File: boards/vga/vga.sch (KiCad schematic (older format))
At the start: 80 parts, among them J1 Conn_02x20_Odd_Even, J2 L77HDE15SD1CH4RHNVGA, Q1 BSS84AK, U1 SN74LV161APW, U10 62256-TSOP, U11 SN74LV161APW, U12 SN74LV161APW, U13 SN74LV244APW, U14 SN74LV20APW, U15 74LV32APWJ, U16 74LV08APWJ, U17 AT28C256-PLCC32, U18 SN74LV273APW, U19 SN74LV273APW, U2 SN74LV161APW, U20 CD74AC151M96, U21 SN74LV157APW, U22 SN74LV10APW, U23 SN74LV74APW, U24 SN74LV00APW, U25 74LV32APWJ, U26 SN74LV21APW, U27 SN74AHC1G86DBVR, U28 74LV32APWJ, U29 74LV08APWJ, U3 SN74LV157APW, U30 SN74LV74APW, U4 SN74LV157APW, U5 SN74LV157APW, U6 SN74LV161APW, U7 SN74LV161APW, U8 SN74LV244APW, U9 62256-TSOP, X1 MXO45HS-3C-25M1750

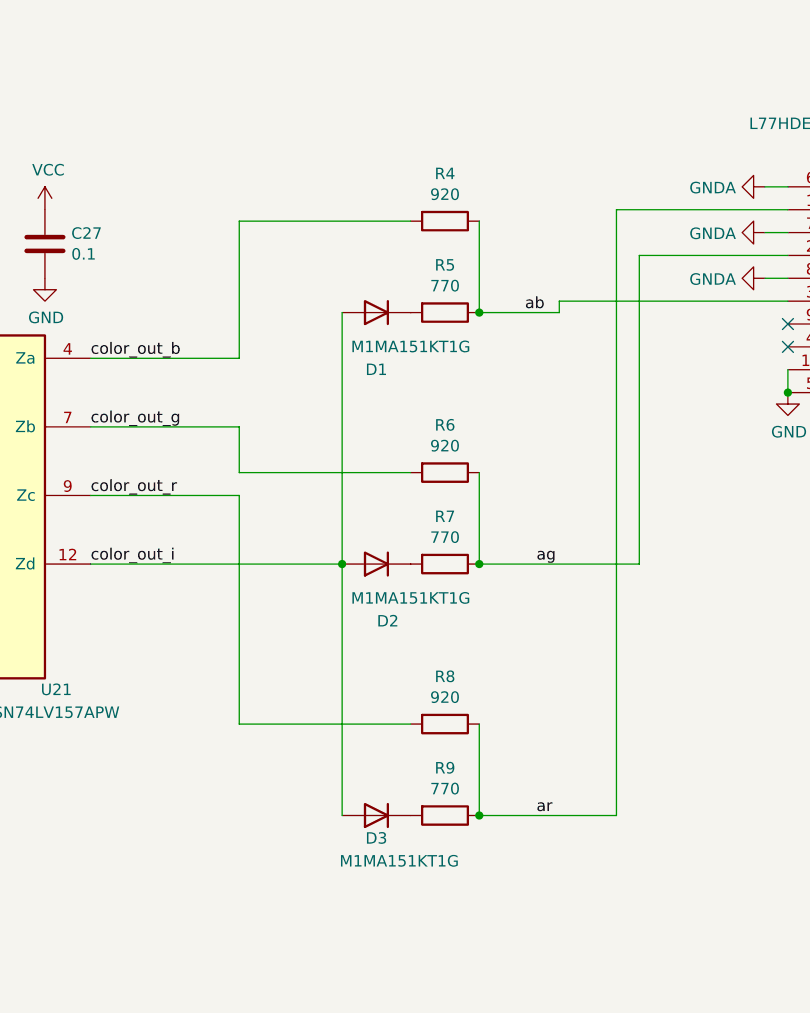
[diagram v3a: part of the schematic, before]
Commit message: VGA: DAC diode array and trim potentiometers
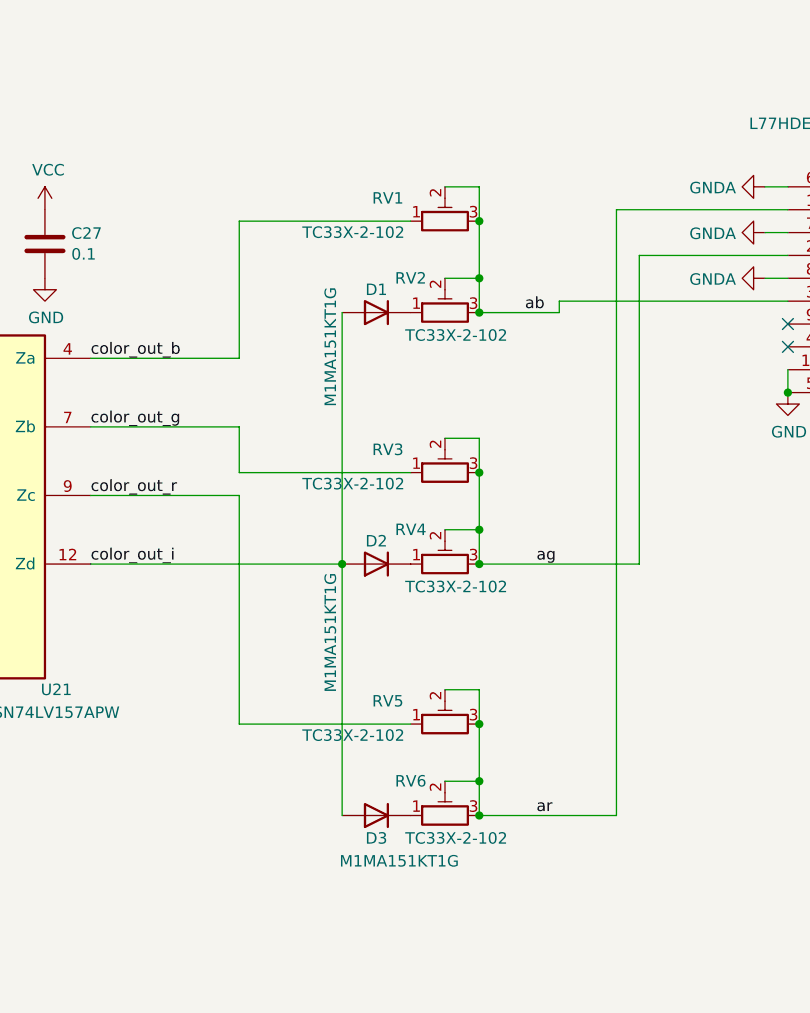
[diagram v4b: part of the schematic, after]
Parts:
- removed R4, R6, R8: 920, symbol Device:R
- removed R5, R7, R9: 770, symbol Device:R
- added RV1, RV2, RV3, RV4, RV5, RV6: TC33X-2-102, Potentiometer_SMD:Potentiometer_Bourns_TC33X_Vertical, symbol Device:R_POT_TRIM
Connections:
- net ab: now also RV1.2, RV1.3, RV2.2, RV2.3
- net ag: now also RV3.2, RV3.3, RV4.2, RV4.3
- net ar: now also RV5.2, RV5.3, RV6.2, RV6.3
- net color_out_b: now also RV1.1
- net color_out_g: now also RV3.1
- net color_out_r: now also RV5.1
- net at D1.1 (K): now also RV2.1
- net at D2.1 (K): now also RV4.1
- net at D3.1 (K): now also RV6.1
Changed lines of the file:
@@
 U 1 1 5FEACDCC
 P 19700 4450
-F 0 "D1" H 19700 4700 50  0000 C CNN
-F 1 "M1MA151KT1G" H 19550 4600 50  0000 C CNN
+F 0 "D1" H 19700 4350 50  0000 C CNN
+F 1 "M1MA151KT1G" V 19900 4600 50  0000 C CNN
 F 2 "Diode_SMD:D_SOT-23_ANK" H 19700 4450 50  0001 C CNN
 F 3 "https://www.mouser.de/datasheet/2/308/M1MA151KT1_D-1810723.pdf" H 19700 4450 50  0001 C CNN
@@
 	-1   0    0    1
 $EndComp
-$Comp
-L Device:R R5
-U 1 1 5FEB1B5A
-P 20000 4450
-F 0 "R5" V 19793 4450 50  0000 C CNN
-F 1 "770" V 19884 4450 50  0000 C CNN
-F 2 "" V 19930 4450 50  0001 C CNN
-F 3 "~" H 20000 4450 50  0001 C CNN
-	1    20000 4450
-	0    1    1    0
-$EndComp
-$Comp
-L Device:R R4
-U 1 1 5FEB20CB
-P 20000 4050
-F 0 "R4" V 19793 4050 50  0000 C CNN
-F 1 "920" V 19884 4050 50  0000 C CNN
-F 2 "" V 19930 4050 50  0001 C CNN
-F 3 "~" H 20000 4050 50  0001 C CNN
-	1    20000 4050
-	0    1    1    0
-$EndComp
-Wire Wire Line
-	20150 4450 20150 4050
-Connection ~ 20150 4450
+Wire Wire Line
+	20150 4450 20150 4300
 $Comp
 L power:GNDA #PWR0166
@@
 U 1 1 5FF3DA39
 P 19700 5550
-F 0 "D2" H 19650 5800 50  0000 C CNN
-F 1 "M1MA151KT1G" H 19550 5700 50  0000 C CNN
+F 0 "D2" H 19700 5450 50  0000 C CNN
+F 1 "M1MA151KT1G" V 19900 5850 50  0000 C CNN
 F 2 "Diode_SMD:D_SOT-23_ANK" H 19700 5550 50  0001 C CNN
 F 3 "https://www.mouser.de/datasheet/2/308/M1MA151KT1_D-1810723.pdf" H 19700 5550 50  0001 C CNN
@@
 	-1   0    0    1
 $EndComp
-$Comp
-L Device:R R7
-U 1 1 5FF3DA3F
-P 20000 5550
-F 0 "R7" V 19793 5550 50  0000 C CNN
-F 1 "770" V 19884 5550 50  0000 C CNN
-F 2 "" V 19930 5550 50  0001 C CNN
-F 3 "~" H 20000 5550 50  0001 C CNN
-	1    20000 5550
-	0    1    1    0
-$EndComp
-$Comp
-L Device:R R6
-U 1 1 5FF3DA45
-P 20000 5150
-F 0 "R6" V 19793 5150 50  0000 C CNN
-F 1 "920" V 19884 5150 50  0000 C CNN
-F 2 "" V 19930 5150 50  0001 C CNN
-F 3 "~" H 20000 5150 50  0001 C CNN
-	1    20000 5150
-	0    1    1    0
-$EndComp
-Wire Wire Line
-	20150 5550 20150 5150
-Connection ~ 20150 5550
+Wire Wire Line
+	20150 5550 20150 5400
 $Comp
 L Device:D D3
@@
 	-1   0    0    1
 $EndComp
-$Comp
-L Device:R R9
-U 1 1 5FF5B8A6
-P 20000 6650
-F 0 "R9" V 19793 6650 50  0000 C CNN
-F 1 "770" V 19884 6650 50  0000 C CNN
-F 2 "" V 19930 6650 50  0001 C CNN
-F 3 "~" H 20000 6650 50  0001 C CNN
-	1    20000 6650
-	0    1    1    0
-$EndComp
-$Comp
-L Device:R R8
-U 1 1 5FF5B8AC
-P 20000 6250
-F 0 "R8" V 19793 6250 50  0000 C CNN
-F 1 "920" V 19884 6250 50  0000 C CNN
-F 2 "" V 19930 6250 50  0001 C CNN
-F 3 "~" H 20000 6250 50  0001 C CNN
-	1    20000 6250
-	0    1    1    0
-$EndComp
-Wire Wire Line
-	20150 6650 20150 6250
-Connection ~ 20150 6650
+Wire Wire Line
+	20150 6650 20150 6500
 Wire Wire Line
 	19550 6650 19550 5550
@@
 ar
 NoConn ~ 21500 4500
+$Comp
+L Device:R_POT_TRIM RV1
+U 1 1 5FD795FD
+P 20000 4050
+F 0 "RV1" V 20100 4300 50  0000 C CNN
+F 1 "TC33X-2-102" V 19950 4450 50  0000 C CNN
+F 2 "Potentiometer_SMD:Potentiometer_Bourns_TC33X_Vertical" H 20000 4050 50  0001 C CNN
+F 3 "https://www.mouser.de/datasheet/2/54/tc33-778219.pdf" H 20000 4050 50  0001 C CNN
+	1    20000 4050
+	0    -1   -1   0
+$EndComp
+$Comp
+L Device:R_POT_TRIM RV2
+U 1 1 5FD7B4C1
+P 20000 4450
+F 0 "RV2" V 20150 4600 50  0000 C CNN
+F 1 "TC33X-2-102" V 19900 4400 50  0000 C CNN
+F 2 "Potentiometer_SMD:Potentiometer_Bourns_TC33X_Vertical" H 20000 4450 50  0001 C CNN
+F 3 "https://www.mouser.de/datasheet/2/54/tc33-778219.pdf" H 20000 4450 50  0001 C CNN
+	1    20000 4450
+	0    -1   -1   0
+$EndComp
+Connection ~ 20150 4450
+$Comp
+L Device:R_POT_TRIM RV3
+U 1 1 5FD7D4C9
+P 20000 5150
+F 0 "RV3" V 20100 5400 50  0000 C CNN
+F 1 "TC33X-2-102" V 19950 5550 50  0000 C CNN
+F 2 "Potentiometer_SMD:Potentiometer_Bourns_TC33X_Vertical" H 20000 5150 50  0001 C CNN
+F 3 "https://www.mouser.de/datasheet/2/54/tc33-778219.pdf" H 20000 5150 50  0001 C CNN
+	1    20000 5150
+	0    -1   -1   0
+$EndComp
+$Comp
+L Device:R_POT_TRIM RV4
+U 1 1 5FD7DC16
+P 20000 5550
+F 0 "RV4" V 20150 5700 50  0000 C CNN
+F 1 "TC33X-2-102" V 19900 5500 50  0000 C CNN
+F 2 "Potentiometer_SMD:Potentiometer_Bourns_TC33X_Vertical" H 20000 5550 50  0001 C CNN
+F 3 "https://www.mouser.de/datasheet/2/54/tc33-778219.pdf" H 20000 5550 50  0001 C CNN
+	1    20000 5550
+	0    -1   -1   0
+$EndComp
+Connection ~ 20150 5550
+$Comp
+L Device:R_POT_TRIM RV6
+U 1 1 5FD7E9C9
+P 20000 6650
+F 0 "RV6" V 20150 6800 50  0000 C CNN
+F 1 "TC33X-2-102" V 19900 6600 50  0000 C CNN
+F 2 "Potentiometer_SMD:Potentiometer_Bourns_TC33X_Vertical" H 20000 6650 50  0001 C CNN
+F 3 "https://www.mouser.de/datasheet/2/54/tc33-778219.pdf" H 20000 6650 50  0001 C CNN
+	1    20000 6650
+	0    -1   -1   0
+$EndComp
+Connection ~ 20150 6650
+$Comp
+L Device:R_POT_TRIM RV5
+U 1 1 5FD7F2A0
+P 20000 6250
+F 0 "RV5" V 20100 6500 50  0000 C CNN
+F 1 "TC33X-2-102" V 19950 6650 50  0000 C CNN
+F 2 "Potentiometer_SMD:Potentiometer_Bourns_TC33X_Vertical" H 20000 6250 50  0001 C CNN
+F 3 "https://www.mouser.de/datasheet/2/54/tc33-778219.pdf" H 20000 6250 50  0001 C CNN
+	1    20000 6250
+	0    -1   -1   0
+$EndComp
+Wire Wire Line
+	20000 6100 20150 6100
+Wire Wire Line
+	20150 6100 20150 6250
+Connection ~ 20150 6250
+Wire Wire Line
+	20000 6500 20150 6500
+Connection ~ 20150 6500
+Wire Wire Line
+	20150 6500 20150 6250
+Wire Wire Line
+	20000 5400 20150 5400
+Connection ~ 20150 5400
+Wire Wire Line
+	20150 5400 20150 5150
+Wire Wire Line
+	20000 5000 20150 5000
+Wire Wire Line
+	20150 5000 20150 5150
+Connection ~ 20150 5150
+Wire Wire Line
+	20000 4300 20150 4300
+Connection ~ 20150 4300
+Wire Wire Line
+	20150 4300 20150 4050
+Wire Wire Line
+	20000 3900 20150 3900
+Wire Wire Line
+	20150 3900 20150 4050
 Wire Bus Line
 	11050 5150 11050 5850
@@
 Wire Bus Line
 	6050 4500 6050 10250
+Connection ~ 20150 4050
 $EndSCHEMATC

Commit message: VGA: big capacitor
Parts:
- removed D1, D2, D3: M1MA151KT1G, Diode_SMD:D_SOT-23_ANK, symbol Device:D
- added C31: TAJD476M016UNJV, Capacitor_Tantalum_SMD:CP_EIA-7343-40_Kemet-Y, symbol Device:CP
- added D1: BAS16TW, Package_TO_SOT_SMD:SOT-363_SC-70-6, symbol Diode:BAS16TW
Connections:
- net GND: now also C31.2
- net VCC: now also C31.1
- net color_out_i: now also D1.1 (A), D1.2 (A), D1.3 (A)
- net at RV2.1: now also D1.6 (K)
- net at RV4.1: now also D1.5 (K)
- net at RV6.1: now also D1.4 (K)
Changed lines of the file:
@@
 Text Label 22100 4600 0    50   ~ 0
 vsync_out
-$Comp
-L Device:D D1
-U 1 1 5FEACDCC
-P 19700 4450
-F 0 "D1" H 19700 4350 50  0000 C CNN
-F 1 "M1MA151KT1G" V 19900 4600 50  0000 C CNN
-F 2 "Diode_SMD:D_SOT-23_ANK" H 19700 4450 50  0001 C CNN
-F 3 "https://www.mouser.de/datasheet/2/308/M1MA151KT1_D-1810723.pdf" H 19700 4450 50  0001 C CNN
-	1    19700 4450
-	-1   0    0    1
-$EndComp
 Wire Wire Line
 	20150 4450 20150 4300
@@
 Wire Wire Line
 	21400 4100 21500 4100
-$Comp
-L Device:D D2
-U 1 1 5FF3DA39
-P 19700 5550
-F 0 "D2" H 19700 5450 50  0000 C CNN
-F 1 "M1MA151KT1G" V 19900 5850 50  0000 C CNN
-F 2 "Diode_SMD:D_SOT-23_ANK" H 19700 5550 50  0001 C CNN
-F 3 "https://www.mouser.de/datasheet/2/308/M1MA151KT1_D-1810723.pdf" H 19700 5550 50  0001 C CNN
-	1    19700 5550
-	-1   0    0    1
-$EndComp
 Wire Wire Line
 	20150 5550 20150 5400
-$Comp
-L Device:D D3
-U 1 1 5FF5B8A0
-P 19700 6650
-F 0 "D3" H 19700 6750 50  0000 C CNN
-F 1 "M1MA151KT1G" H 19600 6850 50  0000 C CNN
-F 2 "Diode_SMD:D_SOT-23_ANK" H 19700 6650 50  0001 C CNN
-F 3 "https://www.mouser.de/datasheet/2/308/M1MA151KT1_D-1810723.pdf" H 19700 6650 50  0001 C CNN
-	1    19700 6650
-	-1   0    0    1
-$EndComp
 Wire Wire Line
 	20150 6650 20150 6500
@@
 	6050 4500 6050 10250
 Connection ~ 20150 4050
+$Comp
+L Diode:BAS16TW D1
+U 1 1 5FE760D6
+P 19700 4450
+F 0 "D1" H 19850 4350 50  0000 C CNN
+F 1 "BAS16TW" V 19900 4600 50  0000 C CNN
+F 2 "Package_TO_SOT_SMD:SOT-363_SC-70-6" H 19700 4275 50  0001 C CNN
+F 3 "http://www.diodes.com/datasheets/ds30154.pdf" H 19700 4550 50  0001 C CNN
+	1    19700 4450
+	-1   0    0    1
+$EndComp
+$Comp
+L Diode:BAS16TW D1
+U 2 1 5FE78E2D
+P 19700 5550
+F 0 "D1" H 19950 5450 50  0000 C CNN
+F 1 "BAS16TW" V 19900 5750 50  0000 C CNN
+F 2 "Package_TO_SOT_SMD:SOT-363_SC-70-6" H 19700 5375 50  0001 C CNN
+F 3 "http://www.diodes.com/datasheets/ds30154.pdf" H 19700 5650 50  0001 C CNN
+	2    19700 5550
+	-1   0    0    1
+$EndComp
+$Comp
+L Diode:BAS16TW D1
+U 3 1 5FE7C453
+P 19700 6650
+F 0 "D1" H 19950 6650 50  0000 C CNN
+F 1 "BAS16TW" H 19850 6750 50  0000 C CNN
+F 2 "Package_TO_SOT_SMD:SOT-363_SC-70-6" H 19700 6475 50  0001 C CNN
+F 3 "http://www.diodes.com/datasheets/ds30154.pdf" H 19700 6750 50  0001 C CNN
+	3    19700 6650
+	-1   0    0    1
+$EndComp
+$Comp
+L Device:CP C31
+U 1 1 5FE890D9
+P 1800 4200
+F 0 "C31" H 1918 4246 50  0000 L CNN
+F 1 "TAJD476M016UNJV" H 1918 4155 50  0000 L CNN
+F 2 "Capacitor_Tantalum_SMD:CP_EIA-7343-40_Kemet-Y" H 1838 4050 50  0001 C CNN
+F 3 "~" H 1800 4200 50  0001 C CNN
+	1    1800 4200
+	1    0    0    -1
+$EndComp
+$Comp
+L power:VCC #PWR0171
+U 1 1 5FE8AE40
+P 1800 4050
+F 0 "#PWR0171" H 1800 3900 50  0001 C CNN
+F 1 "VCC" V 1815 4177 50  0000 L CNN
+F 2 "" H 1800 4050 50  0001 C CNN
+F 3 "" H 1800 4050 50  0001 C CNN
+	1    1800 4050
+	1    0    0    -1
+$EndComp
+$Comp
+L power:GND #PWR0172
+U 1 1 5FE8B51C
+P 1800 4350
+F 0 "#PWR0172" H 1800 4100 50  0001 C CNN
+F 1 "GND" V 1805 4222 50  0000 R CNN
+F 2 "" H 1800 4350 50  0001 C CNN
+F 3 "" H 1800 4350 50  0001 C CNN
+	1    1800 4350
+	1    0    0    -1
+$EndComp
 $EndSCHEMATC

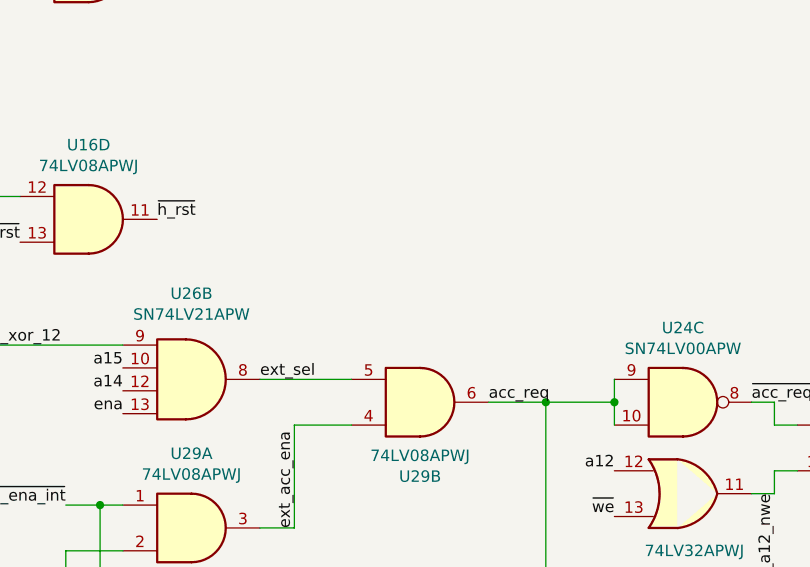
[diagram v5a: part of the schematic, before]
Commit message: VGA: access LED
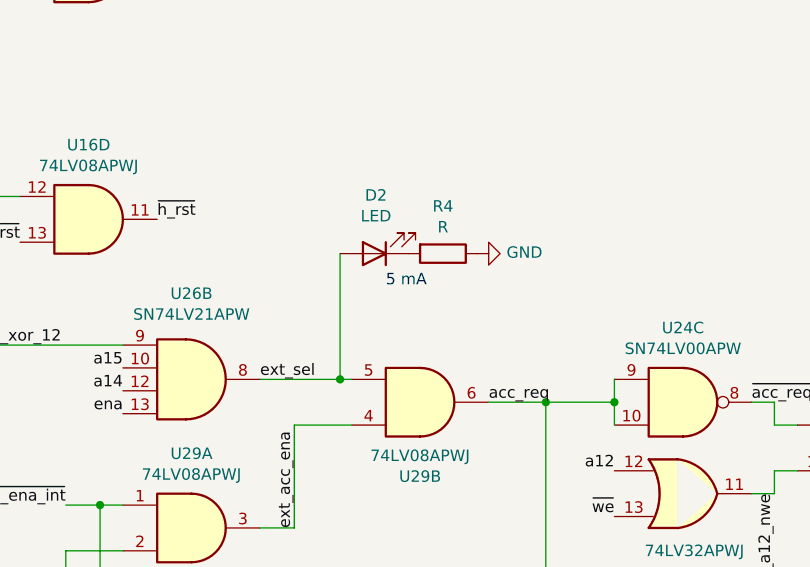
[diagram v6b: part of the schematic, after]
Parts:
- added D2: LED, LED_SMD:LED_0805_2012Metric, symbol Device:LED
- added R4: R, Resistor_SMD:R_0805_2012Metric, symbol Device:R
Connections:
- net GND: now also R4.1
- net ext_sel: now also D2.2 (A)
- new net: D2.1 (K), R4.2
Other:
- note added: "5 mA"
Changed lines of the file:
@@
 hsync_int
 Wire Wire Line
-	16750 12850 16350 12850
+	16750 12850 16700 12850
 Wire Wire Line
 	16350 13500 16500 13500
@@
 Wire Wire Line
 	20150 3900 20150 4050
+Connection ~ 20150 4050
+$Comp
+L Diode:BAS16TW D1
+U 1 1 5FE760D6
+P 19700 4450
+F 0 "D1" H 19850 4350 50  0000 C CNN
+F 1 "BAS16TW" V 19900 4600 50  0000 C CNN
+F 2 "Package_TO_SOT_SMD:SOT-363_SC-70-6" H 19700 4275 50  0001 C CNN
+F 3 "http://www.diodes.com/datasheets/ds30154.pdf" H 19700 4550 50  0001 C CNN
+	1    19700 4450
+	-1   0    0    1
+$EndComp
+$Comp
+L Diode:BAS16TW D1
+U 2 1 5FE78E2D
+P 19700 5550
+F 0 "D1" H 19950 5450 50  0000 C CNN
+F 1 "BAS16TW" V 19900 5750 50  0000 C CNN
+F 2 "Package_TO_SOT_SMD:SOT-363_SC-70-6" H 19700 5375 50  0001 C CNN
+F 3 "http://www.diodes.com/datasheets/ds30154.pdf" H 19700 5650 50  0001 C CNN
+	2    19700 5550
+	-1   0    0    1
+$EndComp
+$Comp
+L Diode:BAS16TW D1
+U 3 1 5FE7C453
+P 19700 6650
+F 0 "D1" H 19950 6650 50  0000 C CNN
+F 1 "BAS16TW" H 19850 6750 50  0000 C CNN
+F 2 "Package_TO_SOT_SMD:SOT-363_SC-70-6" H 19700 6475 50  0001 C CNN
+F 3 "http://www.diodes.com/datasheets/ds30154.pdf" H 19700 6750 50  0001 C CNN
+	3    19700 6650
+	-1   0    0    1
+$EndComp
+$Comp
+L Device:CP C31
+U 1 1 5FE890D9
+P 1800 4200
+F 0 "C31" H 1918 4246 50  0000 L CNN
+F 1 "TAJD476M016UNJV" H 1918 4155 50  0000 L CNN
+F 2 "Capacitor_Tantalum_SMD:CP_EIA-7343-40_Kemet-Y" H 1838 4050 50  0001 C CNN
+F 3 "~" H 1800 4200 50  0001 C CNN
+	1    1800 4200
+	1    0    0    -1
+$EndComp
+$Comp
+L power:VCC #PWR0171
+U 1 1 5FE8AE40
+P 1800 4050
+F 0 "#PWR0171" H 1800 3900 50  0001 C CNN
+F 1 "VCC" V 1815 4177 50  0000 L CNN
+F 2 "" H 1800 4050 50  0001 C CNN
+F 3 "" H 1800 4050 50  0001 C CNN
+	1    1800 4050
+	1    0    0    -1
+$EndComp
+$Comp
+L power:GND #PWR0172
+U 1 1 5FE8B51C
+P 1800 4350
+F 0 "#PWR0172" H 1800 4100 50  0001 C CNN
+F 1 "GND" V 1805 4222 50  0000 R CNN
+F 2 "" H 1800 4350 50  0001 C CNN
+F 3 "" H 1800 4350 50  0001 C CNN
+	1    1800 4350
+	1    0    0    -1
+$EndComp
+$Comp
+L Device:LED D2
+U 1 1 5FEA3864
+P 16850 12300
+F 0 "D2" H 16843 12045 50  0000 C CNN
+F 1 "LED" H 16843 12136 50  0000 C CNN
+F 2 "LED_SMD:LED_0805_2012Metric" H 16850 12300 50  0001 C CNN
+F 3 "~" H 16850 12300 50  0001 C CNN
+	1    16850 12300
+	-1   0    0    1
+$EndComp
+$Comp
+L Device:R R4
+U 1 1 5FEA8E23
+P 17150 12300
+F 0 "R4" V 16943 12300 50  0000 C CNN
+F 1 "R" V 17034 12300 50  0000 C CNN
+F 2 "Resistor_SMD:R_0805_2012Metric" V 17080 12300 50  0001 C CNN
+F 3 "~" H 17150 12300 50  0001 C CNN
+	1    17150 12300
+	0    1    1    0
+$EndComp
+$Comp
+L power:GND #PWR0173
+U 1 1 5FEABACE
+P 17300 12300
+F 0 "#PWR0173" H 17300 12050 50  0001 C CNN
+F 1 "GND" V 17305 12172 50  0000 R CNN
+F 2 "" H 17300 12300 50  0001 C CNN
+F 3 "" H 17300 12300 50  0001 C CNN
+	1    17300 12300
+	0    -1   -1   0
+$EndComp
+Wire Wire Line
+	16700 12300 16700 12850
 Wire Bus Line
 	11050 5150 11050 5850
@@
 Wire Bus Line
 	6050 4500 6050 10250
-Connection ~ 20150 4050
-$Comp
-L Diode:BAS16TW D1
-U 1 1 5FE760D6
-P 19700 4450
-F 0 "D1" H 19850 4350 50  0000 C CNN
-F 1 "BAS16TW" V 19900 4600 50  0000 C CNN
-F 2 "Package_TO_SOT_SMD:SOT-363_SC-70-6" H 19700 4275 50  0001 C CNN
-F 3 "http://www.diodes.com/datasheets/ds30154.pdf" H 19700 4550 50  0001 C CNN
-	1    19700 4450
-	-1   0    0    1
-$EndComp
-$Comp
-L Diode:BAS16TW D1
-U 2 1 5FE78E2D
-P 19700 5550
-F 0 "D1" H 19950 5450 50  0000 C CNN
-F 1 "BAS16TW" V 19900 5750 50  0000 C CNN
-F 2 "Package_TO_SOT_SMD:SOT-363_SC-70-6" H 19700 5375 50  0001 C CNN
-F 3 "http://www.diodes.com/datasheets/ds30154.pdf" H 19700 5650 50  0001 C CNN
-	2    19700 5550
-	-1   0    0    1
-$EndComp
-$Comp
-L Diode:BAS16TW D1
-U 3 1 5FE7C453
-P 19700 6650
-F 0 "D1" H 19950 6650 50  0000 C CNN
-F 1 "BAS16TW" H 19850 6750 50  0000 C CNN
-F 2 "Package_TO_SOT_SMD:SOT-363_SC-70-6" H 19700 6475 50  0001 C CNN
-F 3 "http://www.diodes.com/datasheets/ds30154.pdf" H 19700 6750 50  0001 C CNN
-	3    19700 6650
-	-1   0    0    1
-$EndComp
-$Comp
-L Device:CP C31
-U 1 1 5FE890D9
-P 1800 4200
-F 0 "C31" H 1918 4246 50  0000 L CNN
-F 1 "TAJD476M016UNJV" H 1918 4155 50  0000 L CNN
-F 2 "Capacitor_Tantalum_SMD:CP_EIA-7343-40_Kemet-Y" H 1838 4050 50  0001 C CNN
-F 3 "~" H 1800 4200 50  0001 C CNN
-	1    1800 4200
-	1    0    0    -1
-$EndComp
-$Comp
-L power:VCC #PWR0171
-U 1 1 5FE8AE40
-P 1800 4050
-F 0 "#PWR0171" H 1800 3900 50  0001 C CNN
-F 1 "VCC" V 1815 4177 50  0000 L CNN
-F 2 "" H 1800 4050 50  0001 C CNN
-F 3 "" H 1800 4050 50  0001 C CNN
-	1    1800 4050
-	1    0    0    -1
-$EndComp
-$Comp
-L power:GND #PWR0172
-U 1 1 5FE8B51C
-P 1800 4350
-F 0 "#PWR0172" H 1800 4100 50  0001 C CNN
-F 1 "GND" V 1805 4222 50  0000 R CNN
-F 2 "" H 1800 4350 50  0001 C CNN
-F 3 "" H 1800 4350 50  0001 C CNN
-	1    1800 4350
-	1    0    0    -1
-$EndComp
+Connection ~ 16700 12850
+Wire Wire Line
+	16700 12850 16350 12850
+Text Notes 16900 12450 0    50   ~ 0
+5 mA
 $EndSCHEMATC
